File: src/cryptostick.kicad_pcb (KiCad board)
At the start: 2 copper layers, 21.8 x 16.3 mm, 37 parts, among them J1 SIM_JACKET, J2 USB_A, P1 CONN_4, U1 STM32F103TB, U2 CAT6217-330, U3 DF5A5.6JE, X1 12MHz, p1 debug-pin, p2 debug-pin, p3 debug-pin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

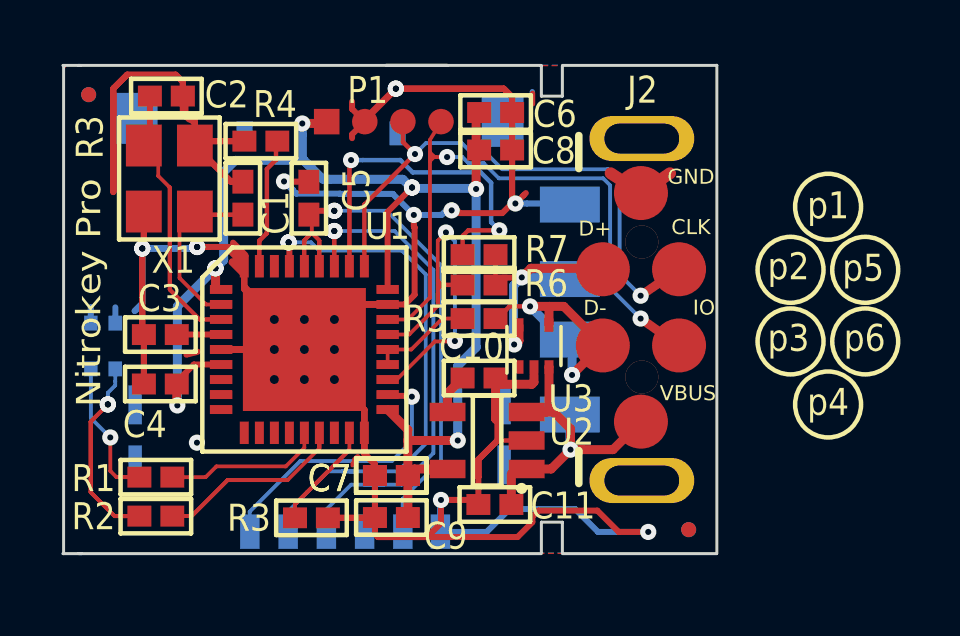
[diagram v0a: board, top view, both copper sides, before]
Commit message: Modifications for pro rev4 with BGA
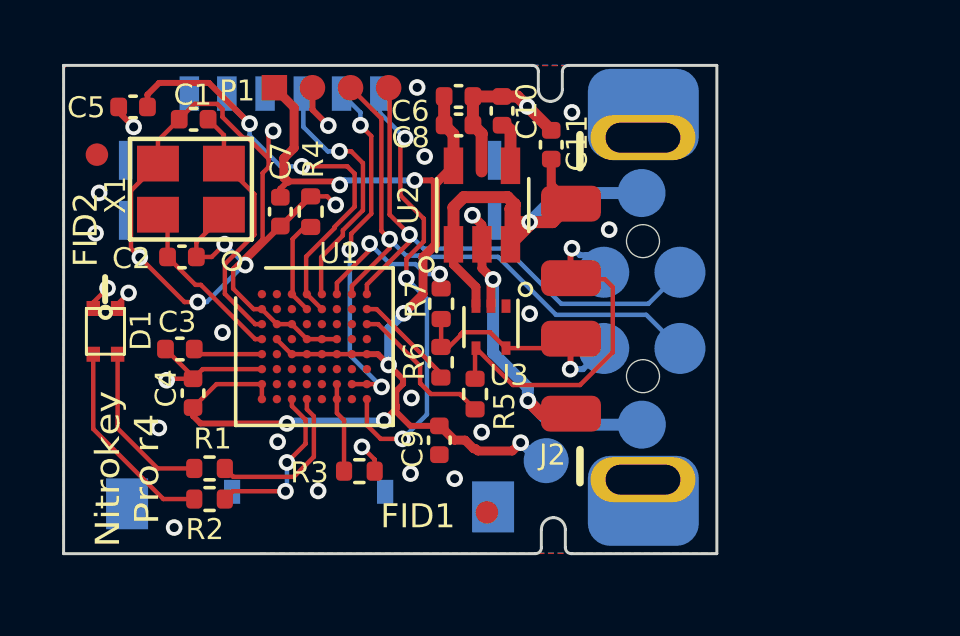
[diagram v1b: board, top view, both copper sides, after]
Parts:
- removed the C7 at (125.7, 104.5)
- removed REF** (x3): Fiducial_0.5mm_Dia_1mm_Outer, footprints:Fiducial_0.5mm_Dia_1mm_Outer
- removed REF**: Fiducial_0.5mm_Dia_1mm_Outer, Fiducial:Fiducial_0.5mm_Dia_1mm_Outer
- added FID1: Fiducial, Fiducial:Fiducial_0.75mm_Mask1.5mm, F.Cu at (128.8, 105.8)
- added FID2: Fiducial, Fiducial:Fiducial_0.75mm_Mask1.5mm, F.Cu at (115.8, 93.8)
- added TP1: TestPoint, TestPoint:TestPoint_Pad_D1.5mm, B.Cu at (130.8, 104.0)
- C1, C10, C11, C2, C3, C4, C5, C6, C7, C8, C9: footprint c_0402 -> Capacitor_SMD:C_0402_1005Metric
- D1: moved to F.Cu
- R1, R2, R3, R4, R5, R6, R7: footprint r_0402 -> Resistor_SMD:R_0402_1005Metric
- U1: value STM32F103TB -> STM32F103RBHx; footprint QFN36 -> Package_BGA:TFBGA-64_5x5mm_Layout8x8_P0.5mm
- U2: footprint TSOT23-5 -> Package_TO_SOT_SMD:TSOT-23-5
- U3: footprint TO_SOT_Packages_SMD:SOT-553 -> Package_TO_SOT_SMD:SOT-553
- p1, p2, p3, p4, p5, p6: moved to B.Cu
- moved C11 12.1 mm to (131.0, 93.5), turned to 90 degrees
- moved C7 9.54 mm to (122.0, 95.8), turned to 90 degrees
- moved C10 8.94 mm to (129.3, 92.4), turned to 90 degrees
- moved U2 7.85 mm to (128.7, 95.5)
- moved p1 7.72 mm to (134.0, 102.8)
- moved p4 7.62 mm to (134.0, 95.1)
- moved C5 6.60 mm to (117.0, 92.3), turned to 180 degrees
- moved C2 5.39 mm to (118.7, 97.3), turned to 0 degrees
- moved C1 3.10 mm to (119.1, 92.7), turned to 180 degrees
- moved C9 3.03 mm to (127.2, 103.4), turned to 270 degrees
- moved R4 2.88 mm to (123.0, 95.8), turned to 90 degrees
- moved R6 2.87 mm to (127.3, 100.8), turned to 90 degrees
- moved p2 2.64 mm to (132.7, 100.3)
- moved p5 2.64 mm to (135.3, 100.3)
- moved R5 2.52 mm to (128.4, 101.8), turned to 90 degrees
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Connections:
- J1 pad 6: (no net) -> Net-(J1-Pad6)
- R1 pad 2: N-000008 -> /LED1
- R2 pad 2: N-0000020 -> /LED2
- U3 pad 1: (no net) -> Net-(U3-Pad1)
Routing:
- net GND: track 160.0 -> 61.0 mm, vias 13 -> 32
- net +3.3V: track 54.2 -> 42.1 mm, vias 8 -> 7
- net N-0000020: track 11.2 -> 0.00 mm
- net /OSC_OUT: track 17.0 -> 5.99 mm
- net /USB_EN: track 15.4 -> 5.40 mm
- net /SCRST: track 18.4 -> 8.56 mm, vias 2 -> 1
- net /D+: track 12.8 -> 3.49 mm, vias 2 -> 0
- net /SCSDA: track 19.1 -> 11.9 mm, vias 2 -> 3
- net /SCCLK: track 9.37 -> 15.4 mm, vias 1 -> 3
- net Net-(D1-Pad4): track 12.8 -> 6.83 mm, vias 2 -> 0
- net /LED2: track 0.00 -> 5.66 mm, vias 0 -> 2
- net /LED1: track 0.00 -> 5.38 mm
- net N-000008: track 5.31 -> 0.00 mm
- net /VBUS: track 11.8 -> 16.9 mm
- net /SCVCC: track 20.6 -> 15.7 mm
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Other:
- outline, holes or cut-outs redrawn
- net class Default: via_dia 0.5461 -> 0.45; via_drill 0.381 -> 0.2
- net class GND removed
- net class VBUS removed
- net class VDD removed
- rule pad_to_mask_clearance: 0.05 -> 0
- rule via_min_drill: 0.381 -> 0.2
- rule via_min_size: 0.5461 -> 0.45
- board text added: "3V3"
- board text added: "Nitrokey Pro r4"
- board text added: "R4"
- board text removed: "R3"

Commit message: Add Rev7 (BGA with smartcard pullup), update production files and panelization script.
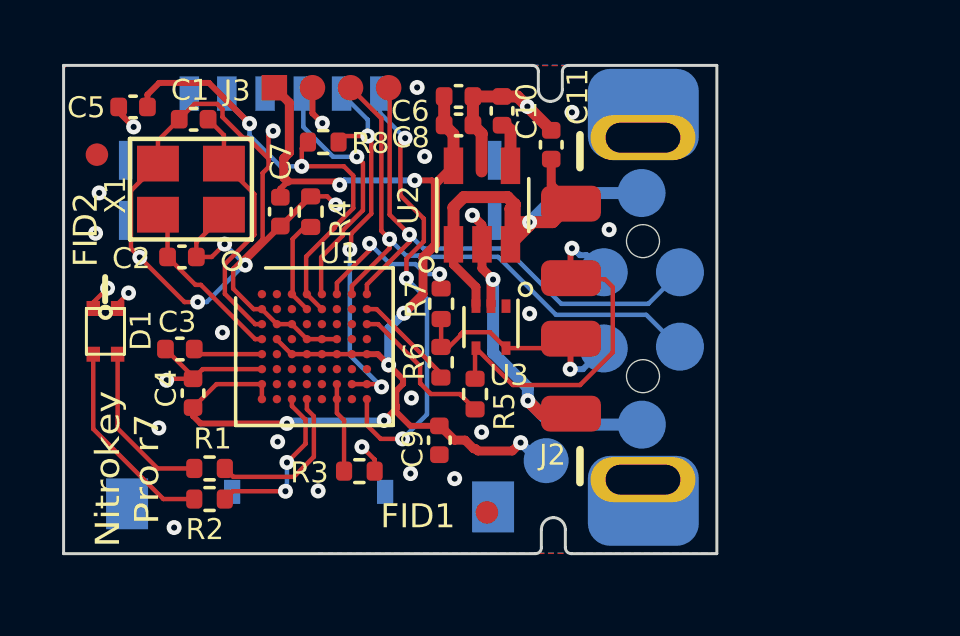
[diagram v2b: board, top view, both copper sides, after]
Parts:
- added R8: 20k, Resistor_SMD:R_0402_1005Metric, F.Cu at (123.4, 93.4)
- renumbered P1 to J3
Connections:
- J1 pad 6: Net-(J1-Pad6) -> unconnected-(J1-NC-Pad6)
- U1 pad A1: Net-(U1-PadA1) -> unconnected-(U1-PC14-PadA1)
- U1 pad A2: Net-(U1-PadA2) -> unconnected-(U1-PC13-PadA2)
- U1 pad B2: Net-(U1-PadB2) -> unconnected-(U1-VBAT-PadB2)
- U1 pad B3: Net-(U1-PadB3) -> unconnected-(U1-PB8-PadB3)
- U1 pad B6: Net-(U1-PadB6) -> unconnected-(U1-PC11-PadB6)
- U1 pad B7: Net-(U1-PadB7) -> unconnected-(U1-PC10-PadB7)
- U1 pad C4: Net-(U1-PadC4) -> unconnected-(U1-PB5-PadC4)
- U1 pad C5: Net-(U1-PadC5) -> unconnected-(U1-PC12-PadC5)
- U1 pad C6: Net-(U1-PadC6) -> unconnected-(U1-PA10-PadC6)
- U1 pad C7: Net-(U1-PadC7) -> unconnected-(U1-PA9-PadC7)
- U1 pad D3: Net-(U1-PadD3) -> unconnected-(U1-PB6-PadD3)
- U1 pad D7: Net-(U1-PadD7) -> unconnected-(U1-PA8-PadD7)
- U1 pad D8: Net-(U1-PadD8) -> unconnected-(U1-PC9-PadD8)
- U1 pad E2: Net-(U1-PadE2) -> unconnected-(U1-PC1-PadE2)
- U1 pad F2: Net-(U1-PadF2) -> unconnected-(U1-PC2-PadF2)
- U1 pad F3: Net-(U1-PadF3) -> unconnected-(U1-PA2-PadF3)
- U1 pad F4: Net-(U1-PadF4) -> unconnected-(U1-PA5-PadF4)
- U1 pad F5: Net-(U1-PadF5) -> unconnected-(U1-PB0-PadF5)
- U1 pad F6: Net-(U1-PadF6) -> unconnected-(U1-PC6-PadF6)
- U1 pad F7: Net-(U1-PadF7) -> unconnected-(U1-PB15-PadF7)
- U1 pad F8: Net-(U1-PadF8) -> unconnected-(U1-PB14-PadF8)
- U1 pad G2: Net-(U1-PadG2) -> unconnected-(U1-PA0-PadG2)
- U1 pad G3: Net-(U1-PadG3) -> unconnected-(U1-PA3-PadG3)
- U1 pad G4: Net-(U1-PadG4) -> unconnected-(U1-PA6-PadG4)
- U1 pad G5: Net-(U1-PadG5) -> unconnected-(U1-PB1-PadG5)
- U1 pad H2: Net-(U1-PadH2) -> unconnected-(U1-PA1-PadH2)
- U1 pad H5: Net-(U1-PadH5) -> unconnected-(U1-PC4-PadH5)
- U1 pad H7: Net-(U1-PadH7) -> unconnected-(U1-PB11-PadH7)
- U3 pad 1: Net-(U3-Pad1) -> unconnected-(U3-C1-Pad1)
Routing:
- net /SCSDA: track 11.9 -> 13.0 mm
- net /SCVCC: track 15.7 -> 16.5 mm
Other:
- net class Default removed
- board text added: "Nitrokey Pro r7"
- board text added: "R7"
- board text removed: "Nitrokey Pro r4"
- board text removed: "R4"
